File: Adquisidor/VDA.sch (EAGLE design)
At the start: 135 parts, among them J1 USB-2.0, J2 STEREO-JACK, J3 FTSH-107-01-L-DV-K-A, J4 CONVERT-1X4-2.54MM-MALE_HOLES, J5 F0504-H-05-10G-R, J6 CONVERT-2X7-2.54MM-FEMALE, Q1 BC856, Q2 BC856, SW1 DSHP03TSGER, U1 SN74LVC1G175, U2 CP2102N-28, U3 STM32F373CBT6, U4 LP5907MFX-3.3/NOPB, U5 ISO7721DR, U6 LP5907MFX-3.3/NOPB, U7 TL072, U8 LM13700

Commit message: trabajando en los panelizados
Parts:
- removed C79: 220n, Property-standar:C_0603
- removed C80: 47u, Property-standar:C_1206
- removed C81: 47u, Property-standar:C-TANTALUM_A_3216
- removed R111: 100k, Property-standar:R_0603
- removed SJ16: (no value), jumper:SJ
- added C32, C39, C40, C41: 100n, Property-standar:C_0603
- added R38: 270, Property-standar:R_0402
- added SJ5: (no value), property-pads:SJ-PSS
- added SJ7: SJUMPER-NC, properti-mechanical:SJUMPER-NC
- C1, C17: value 100n -> 4u7; V (none) -> 16V
- C10, C9: value 10p -> 22u; device Property-standar:C_0603 -> Property-standar:C-ELECT-6.3X5.4
- C11: value 4u7 -> 4.7u
- C14: value 100n -> 47u; device Property-standar:C_0603 -> Property-standar:C-TANTALUM_A_3216
- C15: value 100n -> 47u; device Property-standar:C_0603 -> Property-standar:C_1206; D (none) -> X7R; ESR (none) -> LOW; V (none) -> 10V
- C16: value 100n -> 220n
- C18, C35: V (none) -> 16V
- C19: value 100n -> 10u
- C2: value 470n -> 4u7; V (none) -> 16V
- C21: value 4u7 -> 100n
- C22: value 100n -> 470n
- C24: value 100n -> 4u7; device Property-standar:C_0603 -> Property-standar:C_0805
- C25: value 100n -> 10p
- C26, C4: value 4u7 -> 100n; V 16V -> (none)
- C27: value 10u -> 10p; V 16V -> (none)
- C28: V 16V -> (none)
- C29, C30: DESCRIPTION NP0 -> (none)
- C31: value 47n -> 100n
- C34: value 100n -> 1u; V (none) -> 16V
- C37, C38: value 22u -> 100n; device Property-standar:C-ELECT-6.3X5.4 -> Property-standar:C_0603
- C42: value 1u -> 47n; V 16V -> (none)
- C43: value 100n -> DNP; device Property-standar:C_0603 -> Property-standar:C-ELECT_D8L6.5; V 16V -> (none)
- C5: value 100n -> 4.7u; device Property-standar:C_0603 -> Property-standar:C_0805
- C6, C8: value 4.7u -> 100n; device Property-standar:C_0805 -> Property-standar:C_0603
- D1: value 1N4148 -> LESD5D5.0CT1G; device Property-standar:D-SOD123W -> property:LESD5D5.0CT1G
- D10: value GREEN -> 1N4148; device Property-standar:LED_0603_ARROW -> Property-standar:D-SOD123W
- D11, D12: value ORANGE -> 1N4148; device Property-standar:LED_0603_ARROW -> Property-standar:D-SOD123W
- D16: value 1N4148 -> GREEN; device Property-standar:D-SOD123W -> Property-standar:LED_0603_ARROW
- D17: value 1N4148 -> ORANGE; device Property-standar:D-SOD123W -> Property-standar:LED_0603_ARROW
- D4: value LESD5D5.0CT1G -> D-SOD123W; device property:LESD5D5.0CT1G -> Property-standar:D-SOD123W; TYPE (none) -> Schotky
- D5: value D-SOD123W -> ORANGE; device Property-standar:D-SOD123W -> Property-standar:LED_0603_ARROW; TYPE Schotky -> (none)
- J2: value STEREO-JACK -> CONVERT-1X4-2.54MM-MALE_HOLES; device Connectors:STEREO-JACK -> property-connectors:CONVERT-1X4-2.54MM-MALE_HOLES
- J4: value CONVERT-1X4-2.54MM-MALE_HOLES -> STEREO-JACK; device property-connectors:CONVERT-1X4-2.54MM-MALE_HOLES -> Connectors:STEREO-JACK
- R10: value 150 -> 10k
- R11: value 100 -> 10k
- R12: value 100k -> 270; device Property-standar:R_0603 -> Property-standar:R_0402; TOL (none) -> 1%
- R13: value TBD -> 10k
- R14: value DNP -> 10k
- R17: value 1k -> DNP; device resistor:R-US_R0402 -> Property-standar:R_0603
- R18: value 47.5k -> 33k; device resistor:R-US_R0402 -> Property-standar:R_0603
- R19: value 22.1k -> 10k; device resistor:R-US_R0402 -> Property-standar:R-VARIABLE09VR1B; MPN (none) -> RK09K1110077
- R2: value 10k -> 22.1k; device Property-standar:R_0603 -> resistor:R-US_R0402
- R20, R21: DESCRIPTION (none) -> FILM
- R22: value 270 -> 10M; device Property-standar:R_0402 -> Property-standar:R_0603; DESCRIPTION (none) -> FILM; TOL 1% -> (none)
- R23: value 100 -> 10M
- R24: value 10k -> 100k
- R25, R28: value 10k -> 1k
- R26: value 10k -> 150
- R27: value 10k -> 2k
- R29: value 10k -> 100; device Property-standar:R-VARIABLE09VR1B -> Property-standar:R_0603; MPN RK09K1110077 -> (none)
- R3: value TBD -> 47.5k; device Property-standar:R-VARIABLE-3.2X4 -> resistor:R-US_R0402; MPN 3224W-1-103E -> (none)
- R30: value 33k -> 500; device Property-standar:R_0603 -> Property-standar:R-VARIABLE-3.2X4; MPN (none) -> 3224W-1-501E
- R31: value 3k9 -> 1k
- R32: value 100 -> 500; device Property-standar:R_0603 -> Property-standar:R-VARIABLE-3.2X4; MPN (none) -> 3224W-1-103E
- R33: value 500 -> 100; device Property-standar:R-VARIABLE-3.2X4 -> Property-standar:R_0603; MPN 3224W-1-501E -> (none)
- R34: value 1k -> DNP
- R36: value 270 -> 2k2; device Property-standar:R_0402 -> Property-standar:R_0603; TOL 1% -> (none)
- R37: value 2k2 -> 270; device Property-standar:R_0603 -> Property-standar:R_0402; TOL (none) -> 1%
- R4: value 10M -> 1k; device Property-standar:R_0603 -> resistor:R-US_R0402; DESCRIPTION FILM -> (none)
- R5: value 270 -> 100; device Property-standar:R_0402 -> Property-standar:R_0603; TOL 1% -> (none)
- R6: value 10M -> 100; DESCRIPTION FILM -> (none)
- R7: value TBD -> 100k
- R8: value 100 -> 10k; DESCRIPTION FILM -> (none)
- R9: value 33k -> 10k
- SJ1, SJ2: device property-pads:SJ-PSS -> jumper:SJ
- SJ6: device jumper:SJ -> property-pads:SJ-PSS
- U1: value SN74LVC1G175 -> CP2102N-28; device property_digital:SN74LVC1G175 -> property:CP2102N-28
- U2: value CP2102N-28 -> ISO7721DR; device property:CP2102N-28 -> property_digital:ISO7721DR
- U3: value STM32F373CBT6 -> LP5907MFX-3.3/NOPB; device property:STM32F373-48CT -> property-power:LDO1SOT23-5_1
- U5: value ISO7721DR -> SN74LVC1G175; device property_digital:ISO7721DR -> property_digital:SN74LVC1G175
- U6: value LP5907MFX-3.3/NOPB -> STM32F373CBT6; device property-power:LDO1SOT23-5_1 -> property:STM32F373-48CT
- renumbered S3 to S1, SHIELD to SHIELD1
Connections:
- net +3V3: now also C23.1, C24.1, C26.1, C28.1, C29.1, C33.1, D4.A, J2.4, R10.2, R11.2, R13.2, R8.2, R9.2, SJ1.1, SJ6.NO, U5.VCC, U6.VDD@1, U6.VDD@2; no longer C11.1, C12.1, C13.1, C15.1, C16.1, C3.1, D5.A, J4.4, R2.2, R24.2, R25.2, R26.2, R28.2, SJ1.NO, SJ16.1, U1.VCC, U3.VDD@1, U3.VDD@2
- net +3V3A: now also C30.1, C31.1, C32.1, D14.K, D4.K, R17.2, R19.2, R31.2, SJ2.1, U6.VDDA/VREF+, U6.VDDSD; no longer C14.1, C17.1, C18.1, D16.K, D5.K, R13.2, R14.2, R29.2, SJ6.1, U3.VDDA/VREF+, U3.VDDSD
- net +5V: now also C13.1, C14.+, C15.1, C19.1, C38.1, C6.1, C9.+, D10.K, D12.K, D6.K, R28.2, R37.1, R7.2, SJ6.NC, U2.VCC2, U3.IN; no longer C22.1, C25.1, C27.1, C34.1, C37.+, C80.1, C81.+, D1.K, D13.K, D9.K, R111.2, R34.2, R5.1, SJ1.NC, U5.VCC2, U6.IN
- net -5V: now also C10.-, C37.2, C39.2, C7.2, D11.A; no longer C23.2, C33.2, C35.2, C38.-, D8.A
- net ACQ_LED: now also R38.1, U6.PB6; no longer R36.1, U3.PB6
- net BOOT0: now also R12.1, R14.1, U5.Q, U6.BOOT0; no longer R22.1, R27.1, U1.Q, U3.BOOT0
- net DAC1_CH1: now also R18.2, U6.PA3; no longer R9.2, U3.PA3
- net DAC1_CH2: now also U6.PA4; no longer U3.PA4
- net DAC2_CH1: now also U6.PA5; no longer U3.PA5
- net FF_CLK: now also U5.CLK, U6.PB9; no longer U1.CLK, U3.PB9
- net FF_CLR: now also C22.1, R8.1, U5.!CLR!; no longer C2.1, R2.1, U1.!CLR!
- net FF_D: now also U5.D, U6.PB8; no longer U1.D, U3.PB8
- net GND: now also C10.+, C13.2, C14.-, C21.2, C24.2, C30.2, C31.2, C32.2, C33.2, C35.2, C37.1, C38.2, C39.1, C40.2, C6.2, C7.1, C9.-, D15.A, D16.K, D17.K, D5.K, J2.2, J4.SLEEVE, R14.2, R19.1, R22.1, R26.1, R32.2, R33.2, R34.2, SJ5.NO, U2.GND2, U3.GND, U5.GND, U6.VSS, U6.VSSA/VREF-, U6.VSSD/VREFSD-; no longer C10.2, C11.2, C12.2, C14.2, C2.2, C23.1, C3.2, C33.1, C35.1, C37.-, C38.+, C42.2, C43.2, C79.2, C80.2, C81.-, C9.2, D10.K, D11.K, D12.K, D17.A, J2.SLEEVE, J4.2, R10.1, R11.2, R29.1, R31.2, R4.1, R7.1, SJ2.NO, U1.GND, U3.VSS, U3.VSSA/VREF-, U3.VSSD/VREFSD-, U5.GND2, U6.GND
- net GND-1: now also C11.2, C12.2, C2.2, C3.2, D1.P$2, R3.2, U1.GND, U1.GND@EXP, U2.GND1; no longer C21.2, C24.2, C6.2, C7.2, D4.P$2, R18.2, U2.GND, U2.GND@EXP, U5.GND1
- net JCLK: now also J2.3, U6.PA14; no longer J4.3, U3.PA14
- net JTDI: now also U6.PA15; no longer U3.PA15
- net JTDO: now also U6.PB3; no longer U3.PB3
- net JTMS: now also J2.1, U6.PA13; no longer J4.1, U3.PA13
- net MCU_RX: now also R15.2; no longer R20.2
- net MCU_TX: now also R16.2; no longer R21.2
- net N$1: now also C17.1, C18.1, SJ1.2, U3.OUT; no longer C26.1, C28.1, SJ16.2, U6.OUT
- net N$11: now also R28.1; no longer R34.1
- net N$12: now also D12.A, D13.K; no longer D1.A, D6.K
- net N$13: now also R31.1, R32.1; no longer R13.1, R3.1
- net N$14: now also D16.A, R37.2; no longer D10.A, R5.2
- net N$15: now also D5.A, R12.2; no longer D11.A, R22.2
- net N$16: now also D10.A, D11.K, D9.A, J4.TIP, R20.2; no longer D13.A, D14.K, D15.A, J2.TIP, R8.2
- net N$17: now also D6.A, D8.A, D9.K, R21.2, SJ5.NC; no longer D14.A, D15.K, D9.A, R23.2, SJ2.NC
- net N$18: now also R32.C; no longer R3.C
- net N$19: now also R25.2, R27.1; no longer R30.2, R31.1
- net N$2: now also C42.1, C43.+, R24.2, SJ7.P$1; no longer C31.1, R12.2, R35.1
- net N$20: now also R30.2, R30.C; no longer R33.2, R33.C
- net N$22: now also R29.1, R30.1; no longer R32.1, R33.1
- net N$23: now also SJ6.COM; no longer SJ1.COM
- net N$24: now also D13.A, R26.2; no longer D6.A, R10.2
- net N$27: now also R36.1; no longer R37.1
- net N$3: now also C40.1, R21.1, R22.2; no longer C29.1, R23.1, R4.2
- net N$4: now also C41.1, R20.1, R23.2; no longer C30.1, R6.2, R8.1
- net N$46: now also C16.1, R7.1, U3.EN; no longer C79.1, R111.1, U6.EN
- net N$5: now also C43.-, R35.1, SJ7.P$2; no longer R3.2, R7.2
- net N$50: now also C21.1, SJ2.2; no longer C19.1, SJ6.2
- net N$54: now also R4.2, U1.!RST; no longer R17.2, U2.!RST
- net N$6: now also J4.RING, SJ5.COM; no longer J2.RING, SJ2.COM
- net N$7: now also R17.1, R18.1; no longer R14.1, R9.1
- net N$8: now also D17.A, R38.2; no longer D12.A, R36.2
- net N$9: now also R29.2, R33.1, R34.1; no longer R11.1, R32.2
- net NRST: now also C23.2, R9.1, U6.NRST; no longer C13.2, R28.1, U3.NRST
- net OSC2_IN: now also C25.1, U6.PF0/OSC_IN; no longer C9.1, U3.PF0/OSC_IN
- net OSC2_OUT: now also C27.1, U6.PF1/OSC_OUT; no longer C10.1, U3.PF1/OSC_OUT
- net OUT_CHARGE_AMP: now also C41.2, R23.1, R25.1; no longer C30.2, R30.1, R6.1
- net OUT_OTA: now also C42.2, R24.1; no longer C31.2, R12.1
- net POWER_LED: now also U6.PB7; no longer U3.PB7
- net RXD: now also U1.RXD, U2.OUT_A; no longer U2.RXD, U5.OUT_A
- net SDADC1_CH4: now also U6.PB2; no longer U3.PB2
- net SDADC1_CH5: now also D14.A, D15.K, R36.2, U6.PB1; no longer D16.A, D17.K, R37.2, U3.PB1
- net SDADC1_CH6: now also R19.C, U6.PB0; no longer R29.C, U3.PB0
- net SDADC1_CH7: now also U6.PE9; no longer U3.PE9
- net SDADC1_CH8: now also U6.PE8; no longer U3.PE8
- net SDADC3_CH7: now also U6.PB15; no longer U3.PB15
- net SDADC3_CH8: now also U6.PB14; no longer U3.PB14
- net SHIELD: now also C3.1; no longer C1.1
- net SW_1: now also R10.1, U6.PC13; no longer R24.1, U3.PC13
- net SW_2: now also R11.1, U6.PC14/OSC32_IN; no longer R25.1, U3.PC14/OSC32_IN
- net SW_3: now also R13.1, U6.PC15/OSC32_OUT; no longer R26.1, U3.PC15/OSC32_OUT
- net TXD: now also U1.TXD, U2.IN_B; no longer U2.TXD, U5.IN_B
- net USART_RX: now also R15.1, R6.2, U6.PA10; no longer R15.2, R20.1, U3.PA10
- net USART_TX: now also R16.1, R5.2, U6.PA9; no longer R16.2, R21.1, U3.PA9
- net USB_DET: now also R2.1, R3.1, U1.VBUS; no longer R18.1, R19.1, U2.VBUS
- net USB_DN: now also D3.P$1, U1.D-; no longer D4.P$1, U2.D-
- net USB_DP: now also D2.P$1, U1.D+; no longer D3.P$1, U2.D+
- net USB_RXD: now also R5.1, U2.INA_A; no longer R16.1, U5.INA_A
- net USB_TXD: now also R6.1, U2.OUT_B; no longer R15.1, U5.OUT_B
- net VDD_BRIDGE: now also C11.1, C8.1, R4.1, U1.VDD; no longer C5.1, C6.1, R17.1, U2.VDD
- net VREF_SDADC: now also C34.1, C35.1, U6.VREFSD+; no longer C42.1, C43.1, U3.VREFSD+
- net VUSB: now also C1.1, C12.1, C2.1, C5.1, D1.P$1, R2.2, U1.REGIN, U2.VCC1; no longer C21.1, C24.1, C7.1, C8.1, D2.P$1, R19.2, U2.REGIN, U5.VCC1

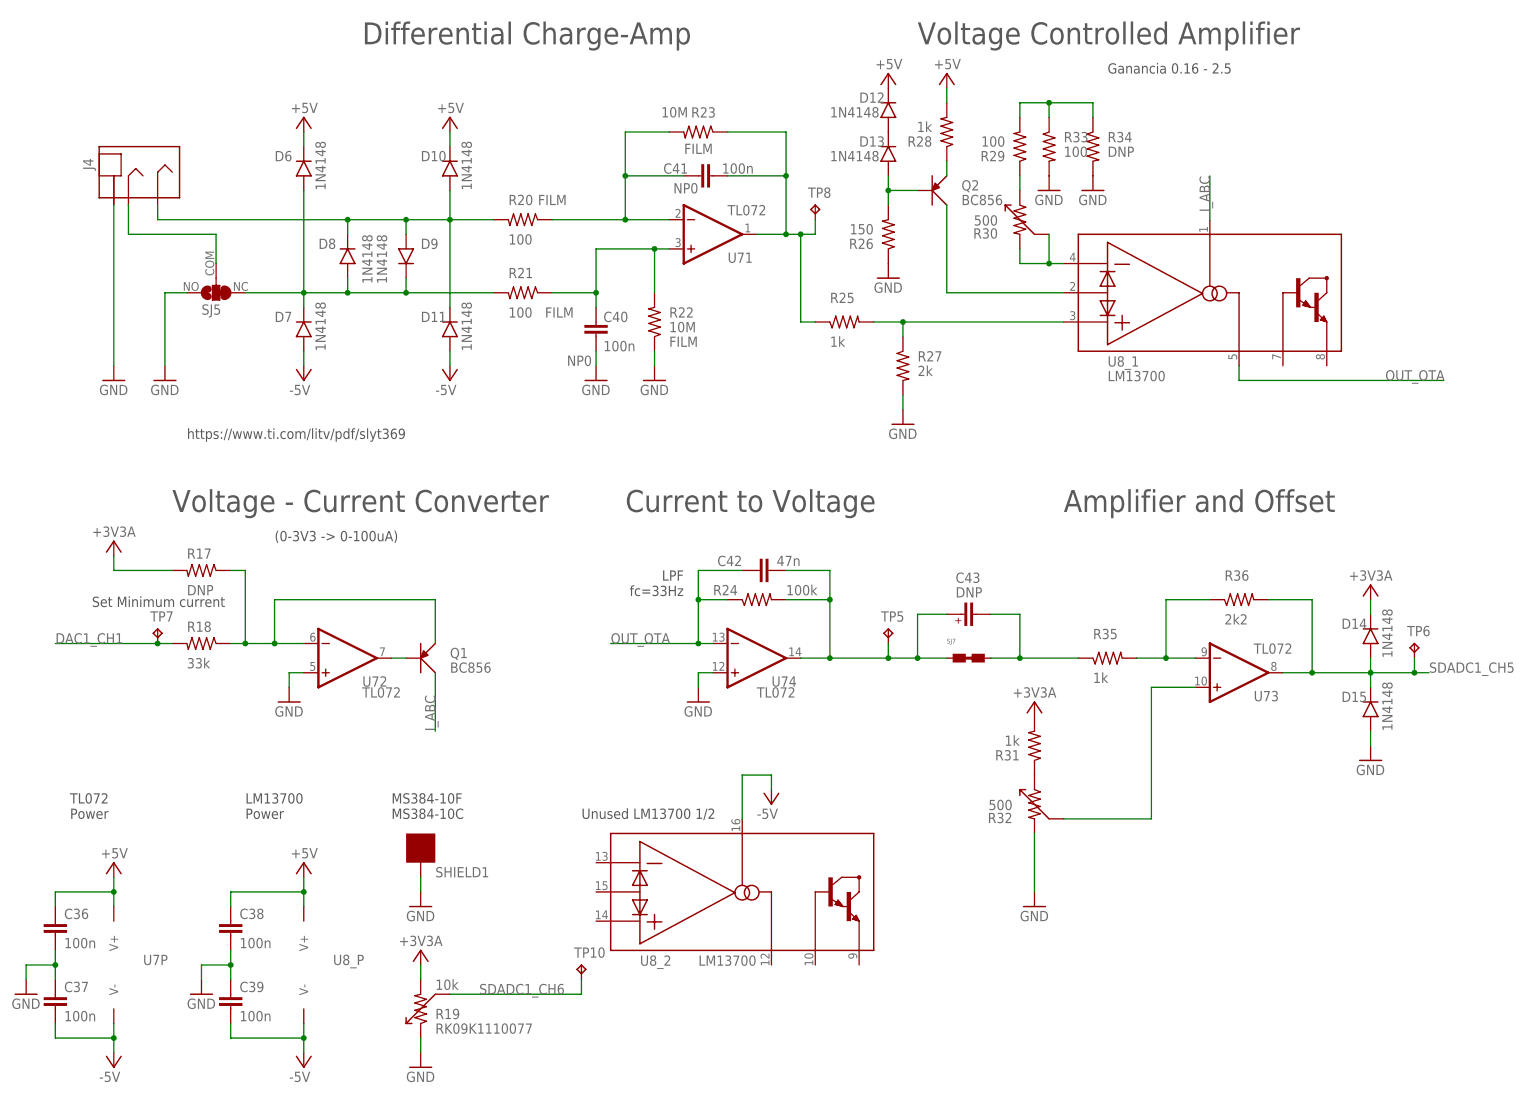
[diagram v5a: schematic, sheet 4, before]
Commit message: BOM del adquisidor listo
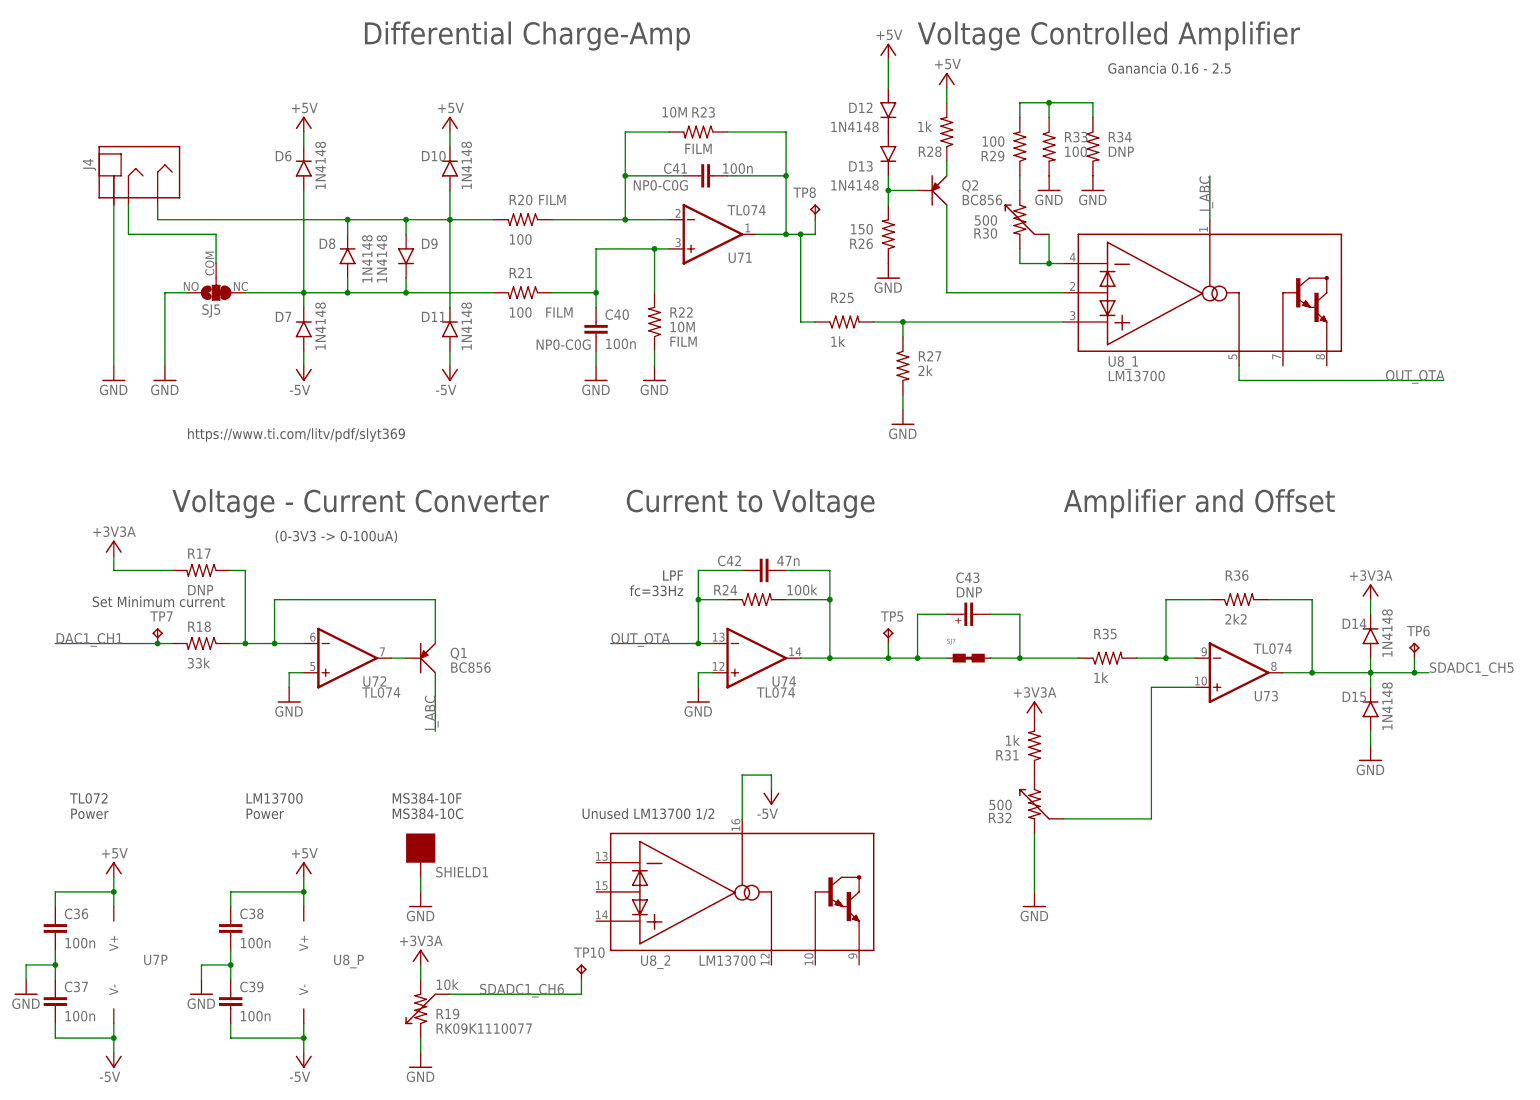
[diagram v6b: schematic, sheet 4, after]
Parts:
- C1, C17, C2, C20: value 4u7 -> 4.7u; device Property-standar:C_0603 -> Property-standar:C_0805; V 16V -> (none)
- C19: value 10u -> 4.7u; device Property-standar:C_0603 -> Property-standar:C_0805; V 16V -> (none)
- C22: value 470n -> 220n
- C40, C41: device Property-standar:C_0603 -> Property-standar:C_1206; DESCRIPTION NP0 -> NP0-C0G
- R12, R37, R38: device Property-standar:R_0402 -> Property-standar:R_0603; TOL 1% -> (none)
- R32: MPN 3224W-1-103E -> 3224W-1-501E
- U7: value TL072 -> TL074
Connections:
- net +5V: now also D12.A; no longer D12.K
- net N$12: now also D12.K, D13.A; no longer D12.A, D13.K
- net N$24: now also D13.K; no longer D13.A
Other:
- note added: "If the VDD and VDDA pins are split, the designer must ensure that VDDA power is applied before or simultaneously with VDD"
- note removed: "Fault"
- note removed: "VERIFICAR QUE TX-RX ESTEN CORRECTOS VERIFICAR CORRECTA ORIENTACION DE IN-OUT AISLADOR"
- moved on the sheet: D12, D13
